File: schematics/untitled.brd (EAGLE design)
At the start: 68.6 x 53.3 mm, 9 parts, among them IC2 L293D

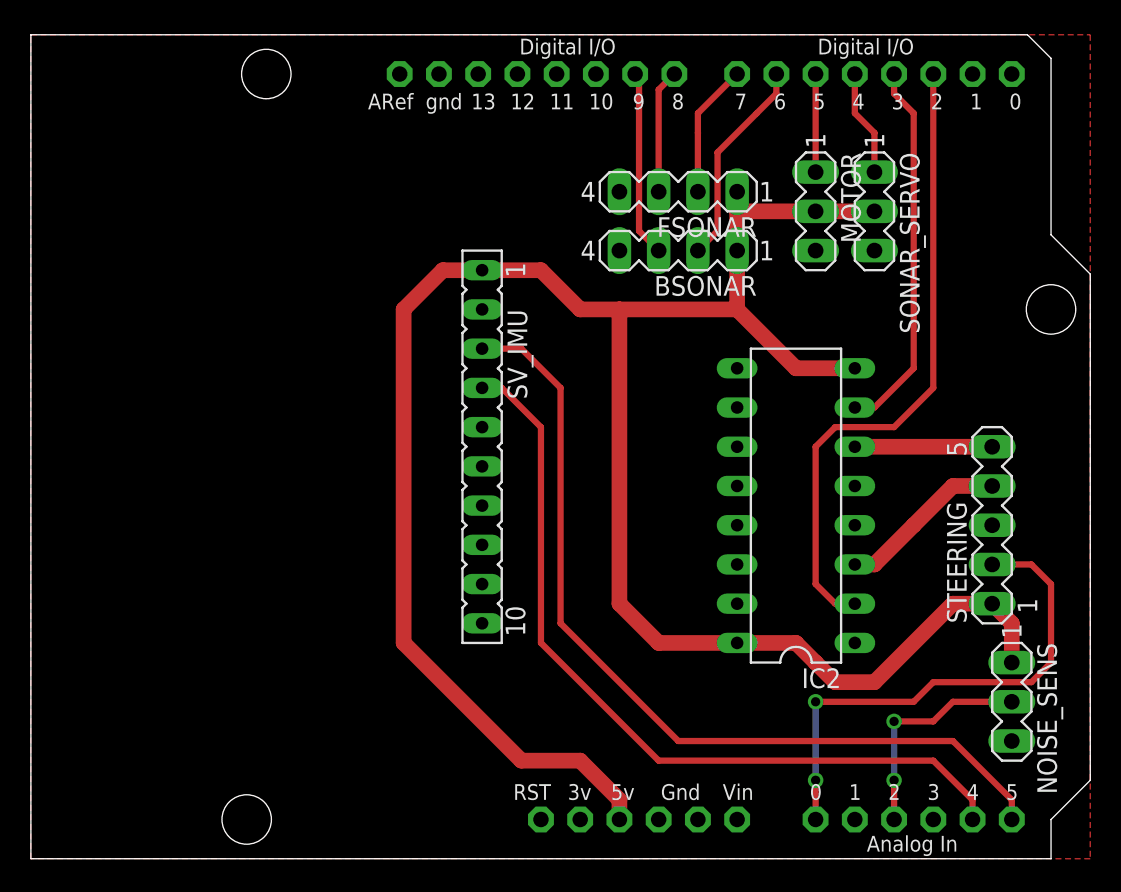
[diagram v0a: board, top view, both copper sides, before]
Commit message: Changed schematics and pcb - new connectors, new arduino pins
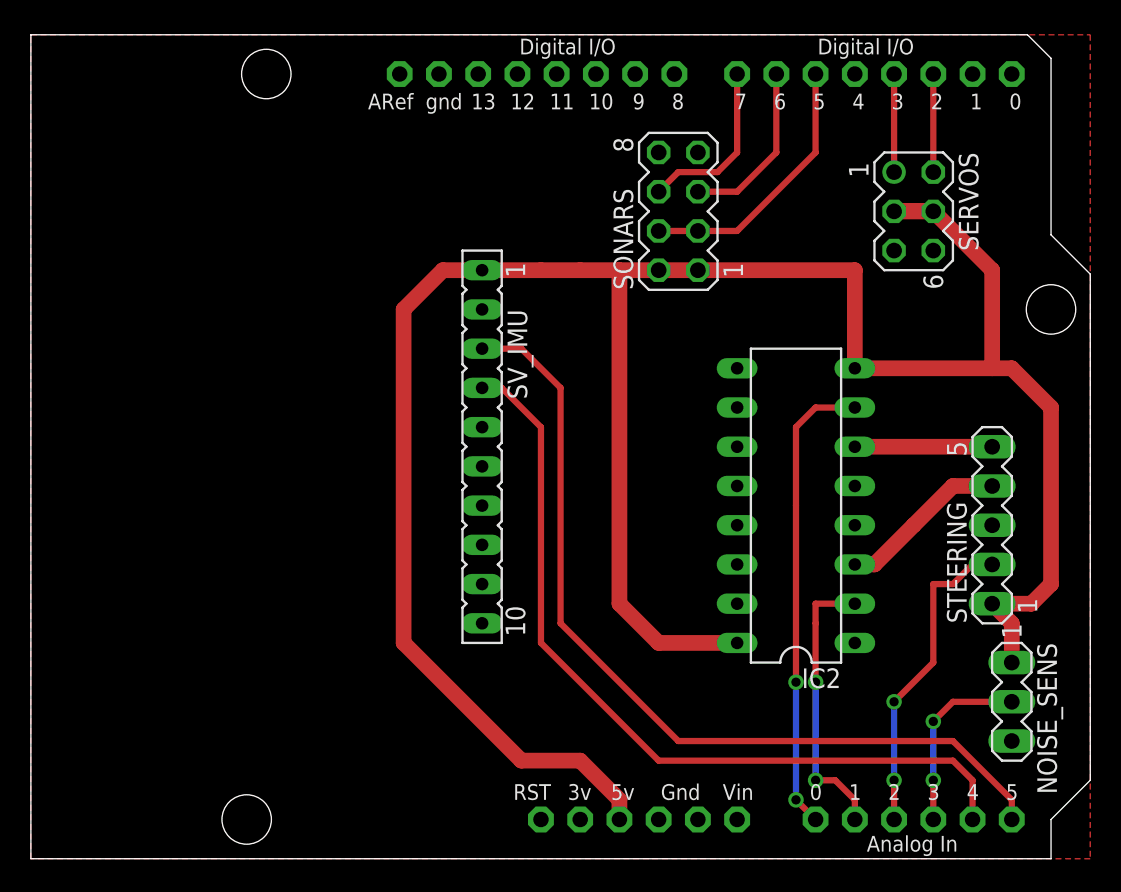
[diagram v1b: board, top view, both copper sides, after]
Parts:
- removed BSONAR, FSONAR: (no value), con-lstb:MA04-1
- removed MOTOR, SONAR_SERVO: (no value), con-lstb:MA03-1
- added SERVOS: (no value), con-lstb:MA03-2
- added SONARS: (no value), con-lstb:MA04-2
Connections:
- removed net B_TRIG: BSONAR.2, U$1.D6
- removed net F_TRIG: FSONAR.2, U$1.D7
- new net SONAR_TRIG: SONARS.3, SONARS.4, U$1.D5
- net +5V: now also SERVOS.3, SERVOS.4, SONARS.1, SONARS.2; no longer BSONAR.1, FSONAR.1, MOTOR.2, SONAR_SERVO.2
- net B_ECHO: now also SONARS.6, U$1.D7; no longer BSONAR.3, U$1.D9
- net F_ECHO: now also SONARS.5, U$1.D6; no longer FSONAR.3, U$1.D8
- net GND: now also SERVOS.5, SERVOS.6, SONARS.7, SONARS.8; no longer BSONAR.4, FSONAR.4, MOTOR.3, SONAR_SERVO.3
- net M_SIGNAL: now also SERVOS.1, U$1.D3; no longer MOTOR.1, U$1.D5
- net NOISE_IN: now also U$1.A3; no longer U$1.A2
- net STEER_1: now also U$1.A1; no longer U$1.D2
- net STEER_2: now also U$1.A0; no longer U$1.D3
- net STEER_POS: now also U$1.A2; no longer U$1.A0
- net S_SIGNAL: now also SERVOS.2, U$1.D2; no longer SONAR_SERVO.1, U$1.D4
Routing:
- net STEER_1: track 41.5 -> 18.3 mm, vias 0 -> 2
- net SONAR_TRIG: track 0.00 -> 17.3 mm
- net +5V: track 143.4 -> 158.6 mm
- net STEER_POS: track 34.6 -> 20.6 mm
- net B_TRIG: track 13.5 -> 0.00 mm
- net F_TRIG: track 8.67 -> 0.00 mm
- net STEER_2: track 24.4 -> 30.3 mm, vias 0 -> 2
- net F_ECHO: track 8.04 -> 11.2 mm
- net NOISE_IN: track 14.5 -> 12.0 mm
- net B_ECHO: track 12.1 -> 11.2 mm
- net SDA: track 52.3 -> 53.0 mm
- net S_SIGNAL: track 6.88 -> 6.35 mm

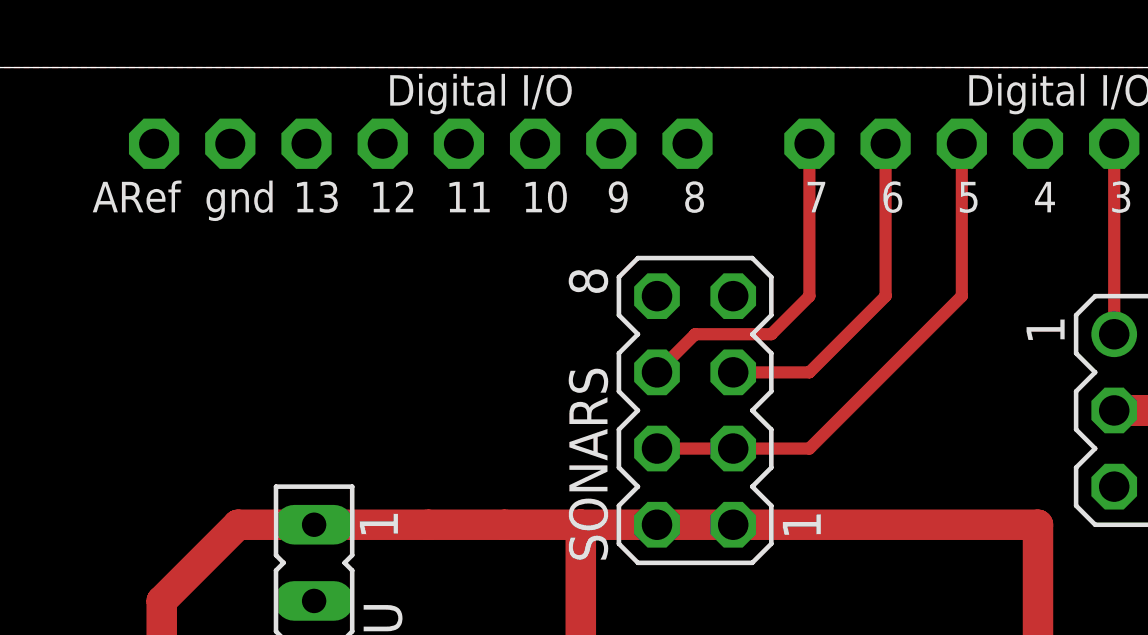
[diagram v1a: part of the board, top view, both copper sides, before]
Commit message: Updated schematics for 2 sonars. Added sonar test. Added makefiles
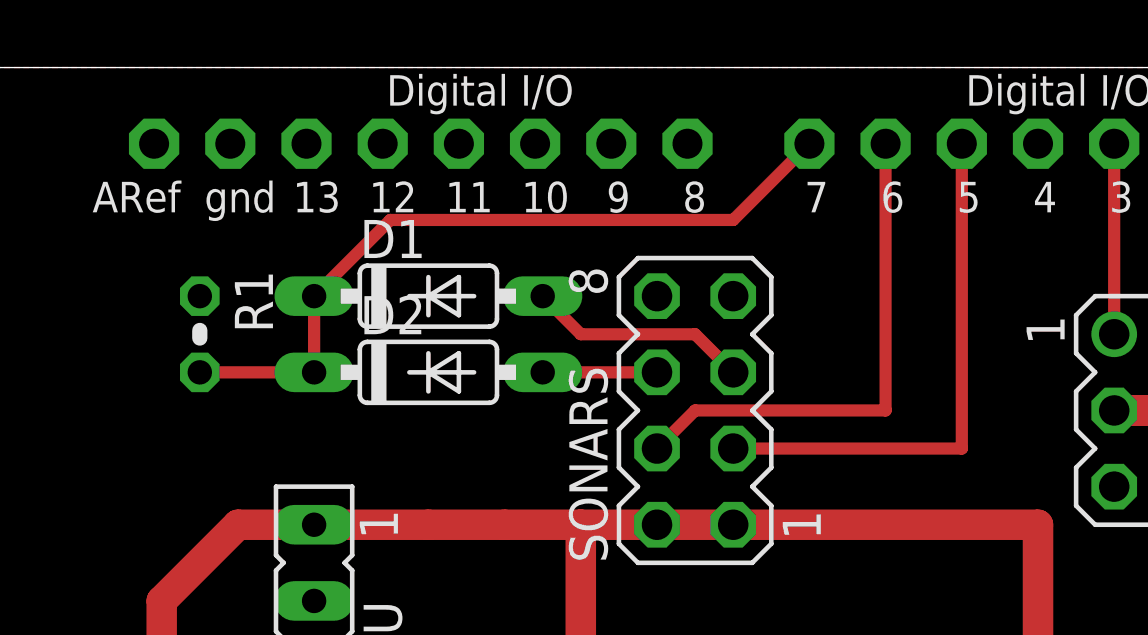
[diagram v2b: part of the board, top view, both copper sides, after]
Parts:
- added D1, D2: 1N4148DO35-7, diode:DO35-7
- added R1: (no value), rcl:0204V
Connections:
- removed net SONAR_TRIG: SONARS.3, SONARS.4, U$1.D5
- new net B_TRIG: SONARS.4, U$1.D6
- new net ECHO: D1.C, D2.C, R1.2, U$1.D7
- new net F_TRIG: SONARS.3, U$1.D5
- net B_ECHO: now also D2.A; no longer U$1.D7
- net F_ECHO: now also D1.A; no longer U$1.D6
- net GND: now also R1.1
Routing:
- net ECHO: track 0.00 -> 25.0 mm
- net F_TRIG: track 0.00 -> 17.8 mm
- net SONAR_TRIG: track 17.3 -> 0.00 mm
- net B_TRIG: track 0.00 -> 17.0 mm
- net B_ECHO: track 11.2 -> 3.81 mm
- net F_ECHO: track 11.2 -> 7.40 mm
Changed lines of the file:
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@@
 <attribute name="OC_FARNELL" value="unknown" x="57.15" y="41.91" size="1.778" layer="27" rot="R270" display="off"/>
 </element>
+<element name="D1" library="diode" package="DO35-7" value="1N4148DO35-7" x="33.02" y="45.72"/>
+<element name="D2" library="diode" package="DO35-7" value="1N4148DO35-7" x="33.02" y="43.18"/>
+<element name="R1" library="rcl" package="0204V" value="" x="25.4" y="44.45" rot="R270"/>
 </elements>
 <signals>
@@
 <contactref element="SONARS" pad="7"/>
 <contactref element="SONARS" pad="8"/>
+<contactref element="R1" pad="1"/>
 </signal>
 <signal name="VIN">
@@
 <signal name="F_ECHO">
 <contactref element="SONARS" pad="5"/>
-<wire x1="43.18" y1="43.18" x2="45.72" y2="43.18" width="0.4064" layer="1"/>
-<wire x1="45.72" y1="43.18" x2="48.26" y2="45.72" width="0.4064" layer="1"/>
-<contactref element="U$1" pad="D6"/>
-<wire x1="48.26" y1="50.8" x2="48.26" y2="45.72" width="0.4064" layer="1"/>
+<contactref element="D1" pad="A"/>
+<wire x1="43.18" y1="43.18" x2="41.91" y2="44.45" width="0.4064" layer="1"/>
+<wire x1="41.91" y1="44.45" x2="38.1" y2="44.45" width="0.4064" layer="1"/>
+<wire x1="38.1" y1="44.45" x2="36.83" y2="45.72" width="0.4064" layer="1"/>
 </signal>
 <signal name="B_ECHO">
 <contactref element="SONARS" pad="6"/>
-<wire x1="40.64" y1="43.18" x2="41.91" y2="44.45" width="0.4064" layer="1"/>
-<wire x1="41.91" y1="44.45" x2="44.45" y2="44.45" width="0.4064" layer="1"/>
-<wire x1="44.45" y1="44.45" x2="45.72" y2="45.72" width="0.4064" layer="1"/>
-<contactref element="U$1" pad="D7"/>
-<wire x1="45.72" y1="50.8" x2="45.72" y2="45.72" width="0.4064" layer="1"/>
+<contactref element="D2" pad="A"/>
+<wire x1="40.64" y1="43.18" x2="36.83" y2="43.18" width="0.4064" layer="1"/>
 </signal>
 <signal name="STEER_POS">
@@
 <wire x1="58.42" y1="2.54" x2="58.42" y2="5.08" width="0.4064" layer="1"/>
 </signal>
-<signal name="SONAR_TRIG">
+<signal name="F_TRIG">
 <contactref element="SONARS" pad="3"/>
-<wire x1="43.18" y1="40.64" x2="45.72" y2="40.64" width="0.4064" layer="1"/>
-<wire x1="45.72" y1="40.64" x2="50.8" y2="45.72" width="0.4064" layer="1"/>
+<contactref element="U$1" pad="D5"/>
+<wire x1="43.18" y1="40.64" x2="50.8" y2="40.64" width="0.4064" layer="1"/>
+<wire x1="50.8" y1="40.64" x2="50.8" y2="50.8" width="0.4064" layer="1"/>
+</signal>
+<signal name="B_TRIG">
 <contactref element="SONARS" pad="4"/>
-<wire x1="40.64" y1="40.64" x2="43.18" y2="40.64" width="0.4064" layer="1"/>
-<contactref element="U$1" pad="D5"/>
-<wire x1="50.8" y1="45.72" x2="50.8" y2="50.8" width="0.4064" layer="1"/>
+<contactref element="U$1" pad="D6"/>
+<wire x1="40.64" y1="40.64" x2="41.91" y2="41.91" width="0.4064" layer="1"/>
+<wire x1="41.91" y1="41.91" x2="48.26" y2="41.91" width="0.4064" layer="1"/>
+<wire x1="48.26" y1="41.91" x2="48.26" y2="50.8" width="0.4064" layer="1"/>
+</signal>
+<signal name="ECHO">
+<contactref element="D2" pad="C"/>
+<contactref element="U$1" pad="D7"/>
+<contactref element="D1" pad="C"/>
+<wire x1="29.21" y1="43.18" x2="29.21" y2="45.72" width="0.4064" layer="1"/>
+<wire x1="29.21" y1="45.72" x2="31.75" y2="48.26" width="0.4064" layer="1"/>
+<wire x1="31.75" y1="48.26" x2="43.18" y2="48.26" width="0.4064" layer="1"/>
+<wire x1="43.18" y1="48.26" x2="45.72" y2="50.8" width="0.4064" layer="1"/>
+<contactref element="R1" pad="2"/>
+<wire x1="25.4" y1="43.18" x2="29.21" y2="43.18" width="0.4064" layer="1"/>
 </signal>
 </signals>

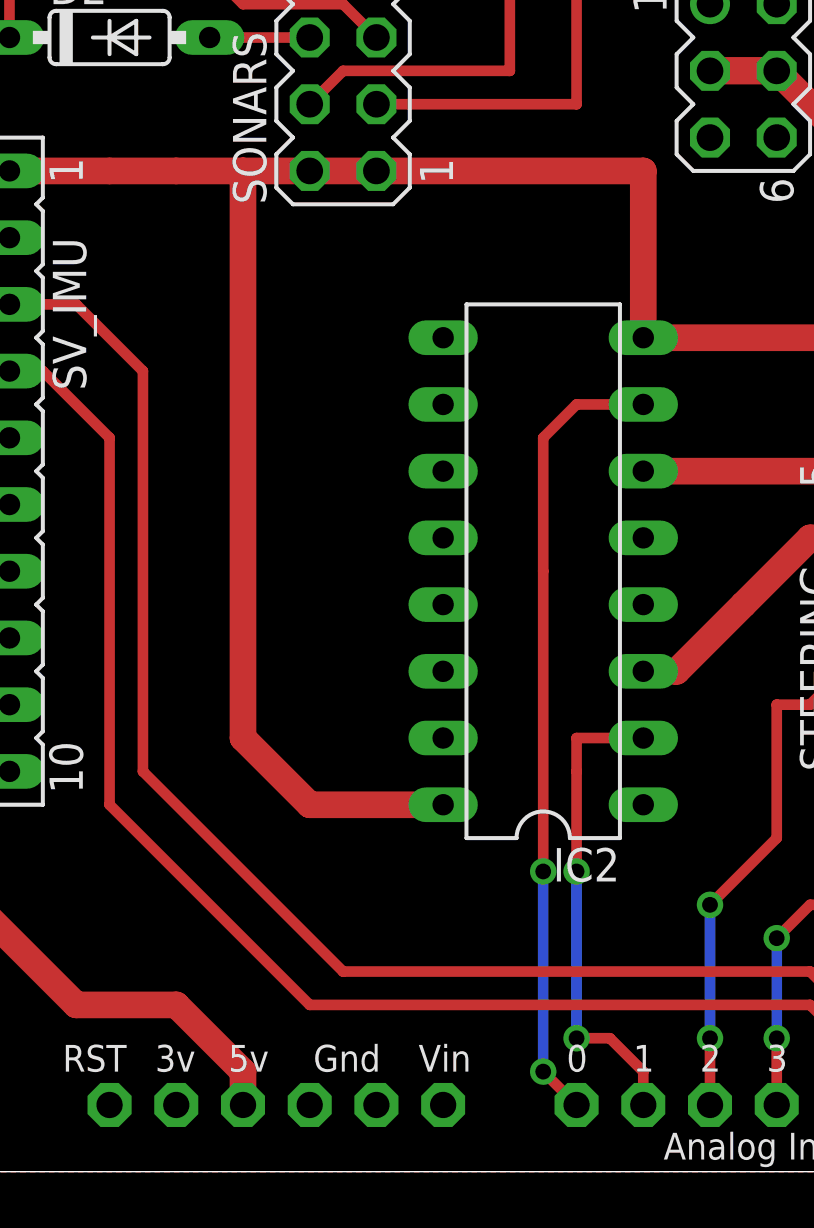
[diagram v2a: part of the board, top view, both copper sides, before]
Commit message: Added power smoothing capacitor
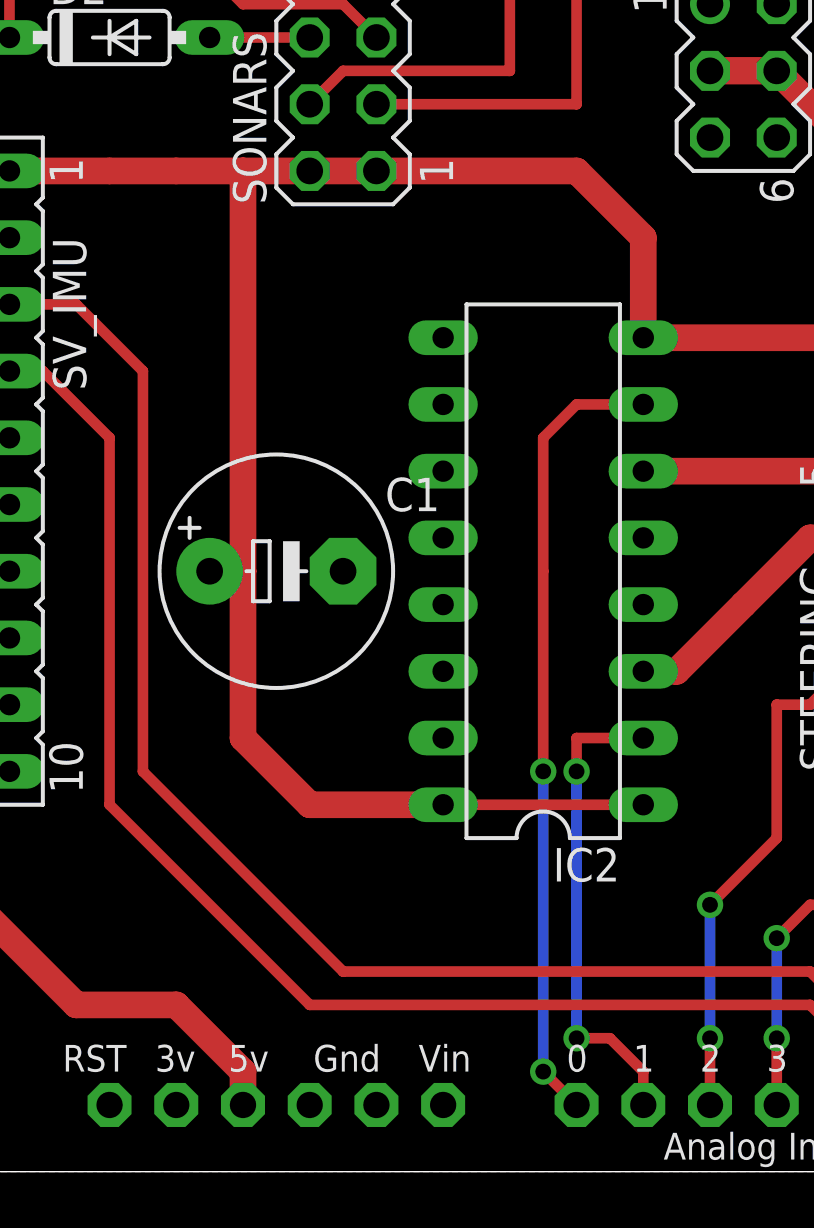
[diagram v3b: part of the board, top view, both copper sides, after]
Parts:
- added C1: 220uF, rcl:E5-8,5
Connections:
- net +5V: now also C1.+, IC2.1
- net GND: now also C1.-
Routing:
- net +5V: track 158.6 -> 166.0 mm
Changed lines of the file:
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@@
 <element name="D2" library="diode" package="DO35-7" value="1N4148DO35-7" x="33.02" y="43.18"/>
 <element name="R1" library="rcl" package="0204V" value="" x="25.4" y="44.45" rot="R270"/>
+<element name="C1" library="rcl" package="E5-8,5" value="220uF" x="39.37" y="22.86"/>
 </elements>
 <signals>
@@
 <contactref element="SONARS" pad="8"/>
 <contactref element="R1" pad="1"/>
+<contactref element="C1" pad="-"/>
 </signal>
 <signal name="VIN">
@@
 <wire x1="45.72" y1="13.97" x2="40.64" y2="13.97" width="1.016" layer="1"/>
 <wire x1="40.64" y1="13.97" x2="38.1" y2="16.51" width="1.016" layer="1"/>
-<wire x1="38.1" y1="16.51" x2="38.1" y2="38.1" width="1.016" layer="1"/>
+<wire x1="38.1" y1="16.51" x2="38.1" y2="22.86" width="1.016" layer="1"/>
+<wire x1="38.1" y1="22.86" x2="38.1" y2="38.1" width="1.016" layer="1"/>
 <wire x1="63.5" y1="12.7" x2="63.5" y2="15.24" width="1.016" layer="1"/>
 <wire x1="63.5" y1="15.24" x2="62.23" y2="16.51" width="1.016" layer="1"/>
@@
 <wire x1="58.42" y1="41.91" x2="62.23" y2="38.1" width="1.016" layer="1"/>
 <wire x1="62.23" y1="38.1" x2="62.23" y2="31.75" width="1.016" layer="1"/>
-<wire x1="43.18" y1="38.1" x2="53.34" y2="38.1" width="1.016" layer="1"/>
-<wire x1="53.34" y1="38.1" x2="53.34" y2="31.75" width="1.016" layer="1"/>
+<wire x1="43.18" y1="38.1" x2="50.8" y2="38.1" width="1.016" layer="1"/>
+<wire x1="50.8" y1="38.1" x2="53.34" y2="35.56" width="1.016" layer="1"/>
+<wire x1="53.34" y1="35.56" x2="53.34" y2="31.75" width="1.016" layer="1"/>
+<contactref element="IC2" pad="1"/>
+<wire x1="53.34" y1="13.97" x2="45.72" y2="13.97" width="0.4064" layer="1"/>
+<contactref element="C1" pad="+"/>
+<wire x1="36.83" y1="22.86" x2="38.1" y2="22.86" width="1.016" layer="1"/>
 </signal>
 <signal name="N$3">
@@
 <wire x1="50.8" y1="29.21" x2="49.53" y2="27.94" width="0.4064" layer="1"/>
 <wire x1="49.53" y1="27.94" x2="49.53" y2="22.86" width="0.4064" layer="1"/>
-<wire x1="49.53" y1="22.86" x2="49.53" y2="11.43" width="0.4064" layer="1"/>
-<via x="49.53" y="11.43" extent="1-16" drill="0.6" shape="square"/>
-<wire x1="49.53" y1="11.43" x2="49.53" y2="3.81" width="0.4064" layer="16"/>
+<wire x1="49.53" y1="22.86" x2="49.53" y2="15.24" width="0.4064" layer="1"/>
+<via x="49.53" y="15.24" extent="1-16" drill="0.6" shape="square"/>
+<wire x1="49.53" y1="15.24" x2="49.53" y2="3.81" width="0.4064" layer="16"/>
 <via x="49.53" y="3.81" extent="1-16" drill="0.6" shape="square"/>
 <wire x1="49.53" y1="3.81" x2="50.8" y2="2.54" width="0.4064" layer="1"/>
@@
 <wire x1="53.34" y1="16.51" x2="50.8" y2="16.51" width="0.4064" layer="1"/>
 <wire x1="50.8" y1="16.51" x2="50.8" y2="15.24" width="0.4064" layer="1"/>
-<wire x1="50.8" y1="15.24" x2="50.8" y2="11.43" width="0.4064" layer="1"/>
-<via x="50.8" y="11.43" extent="1-16" drill="0.6" shape="square"/>
-<wire x1="50.8" y1="11.43" x2="50.8" y2="5.08" width="0.4064" layer="16"/>
+<via x="50.8" y="15.24" extent="1-16" drill="0.6" shape="square"/>
+<wire x1="50.8" y1="15.24" x2="50.8" y2="5.08" width="0.4064" layer="16"/>
 <via x="50.8" y="5.08" extent="1-16" drill="0.6" shape="square"/>
 <wire x1="50.8" y1="5.08" x2="52.07" y2="5.08" width="0.4064" layer="1"/>
